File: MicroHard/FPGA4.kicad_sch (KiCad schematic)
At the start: 0 parts

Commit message: fpg
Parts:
- added U4: XC7A100T-FTG256, symbol FPGA_Xilinx_Artix7:XC7A100T-FTG256
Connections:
- new net +1V0: U4.F7 (VCCINT), U4.F9 (VCCINT), U4.G6 (VCCINT), U4.H9 (VCCINT), U4.J6 (VCCINT), U4.K9 (VCCINT), U4.L8 (VCCINT)
- new net GND: U4.A1 (GND), U4.A11 (GND), U4.B8 (GND), U4.C15 (GND), U4.C5 (GND), U4.D12 (GND), U4.D2 (GND), U4.E9 (GND), U4.F10 (GND), U4.F16 (GND), U4.F6 (GND), U4.G13 (GND), U4.G3 (GND), U4.G9 (GND), U4.H6 (GND), U4.J11 (GND), U4.J9 (GND), U4.K14 (GND), U4.K4 (GND), U4.K6 (GND), U4.L1 (GND), U4.L11 (GND), U4.M8 (GND), U4.N15 (GND), U4.N5 (GND), U4.P12 (GND), U4.P2 (GND), U4.R9 (GND), U4.T16 (GND), U4.T6 (GND)

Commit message: extra files
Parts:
- added C20: 330u, symbol Device:C_Polarized_US
- added C21, C22, C23, C24, C25, C26, C36, C37: 4.7u, symbol Device:C
- added C27, C28, C29, C30, C31, C32, C33, C34, C38, C39, C40, C42, C43: 470n, symbol Device:C
- added C35: 47u, symbol Device:C
- added C41: 100u, symbol Device:C_Polarized_US
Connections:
- net +1V0: now also U4.E10 (VCCBRAM), U4.F11 (VCCBRAM), C20.1, C21.1, C22.1, C23.1, C24.1, C25.1, C26.1, C27.1, C28.1, C29.1, C30.1, C31.1, C32.1, C33.1, C34.1, C41.1, C42.1, C43.1
- net GND: now also C20.2, C21.2, C22.2, C23.2, C24.2, C25.2, C26.2, C27.2, C28.2, C29.2, C30.2, C31.2, C32.2, C33.2, C34.2, C35.2, C36.2, C37.2, C38.2, C39.2, C40.2, C41.2, C42.2, C43.2
- net +1V8: now reaches U4.G10 (VCCAUX)
- net +1V8: now also U4.J10 (VCCAUX), U4.K11 (VCCAUX), U4.L10 (VCCAUX), C35.1, C36.1, C37.1, C38.1, C39.1, C40.1
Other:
- note added: "VCCAUX"
- note added: "VCCBRAM"
- note added: "VCCINT"
- moved on the sheet: U4D

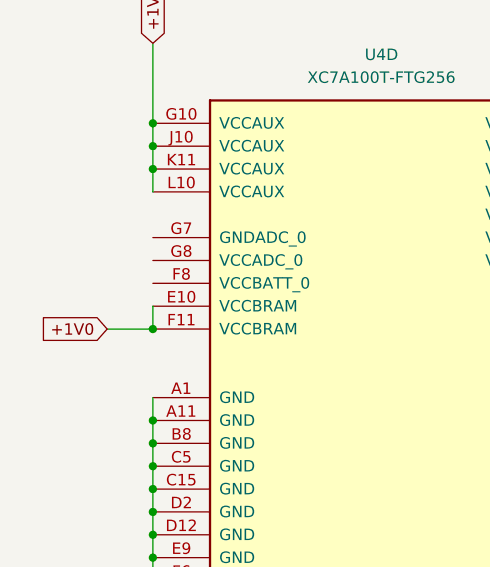
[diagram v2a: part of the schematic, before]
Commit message: feat: finished FPGA config
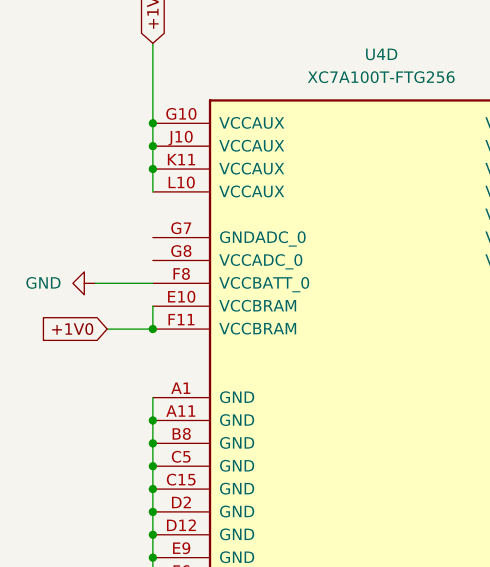
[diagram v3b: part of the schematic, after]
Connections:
- net GND: now also U4.F8 (VCCBATT_0)
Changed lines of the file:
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@@
+	(wire
+		(pts
+			(xy 24.13 76.2) (xy 30.48 76.2)
+		)
+		(stroke
+			(width 0)
+			(type default)
+		)
+	)
 	(wire
 		(pts
@@
 			)
 		)
+	)
+	(symbol
+		(lib_id "power:GND")
+		(at 24.13 76.2 270)
+		(unit 1)
+		(exclude_from_sim no)
+		(in_bom yes)
+		(on_board yes)
+		(dnp no)
+		(fields_autoplaced yes)
+		(property "Reference" "#PWR015"
+			(at 17.78 76.2 0)
+			(effects
+				(font
+					(size 1.27 1.27)
+				)
+				(hide yes)
+			)
+		)
+		(property "Value" "GND"
+			(at 20.32 76.1999 90)
+			(effects
+				(font
+					(size 1.27 1.27)
+				)
+				(justify right)
+			)
+		)
+		(property "Footprint" ""
+			(at 24.13 76.2 0)
+			(effects
+				(font
+					(size 1.27 1.27)
+				)
+				(hide yes)
+			)
+		)
+		(property "Datasheet" ""
+			(at 24.13 76.2 0)
+			(effects
+				(font
+					(size 1.27 1.27)
+				)
+				(hide yes)
+			)
+		)
+		(property "Description" "Power symbol creates a global label with name \"GND\" , ground"
+			(at 24.13 76.2 0)
+			(effects
+				(font
+					(size 1.27 1.27)
+				)
+				(hide yes)
+			)
+		)
+		(pin "1"
+		)
+		(instances
+			(project ""
+				(path "/578bd531-a491-4b15-a479-460d159ffc14/e381883e-e672-4900-88a5-08b94f970a88/ad62afa6-e46e-4108-a891-30710955bca2"
+					(reference "#PWR015")
+					(unit 1)
+				)
+			)
+		)

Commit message: feat: finished Flash mem and FPGA Config
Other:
- note added: "On the physical board the smallest capacitors must be closest to the power input"
- note removed: "VCCAUX"
- note removed: "VCCBRAM"
- note removed: "VCCINT"
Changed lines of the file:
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@@
+	(wire
+		(pts
+			(xy 99.06 85.09) (xy 109.22 85.09)
+		)
+		(stroke
+			(width 0)
+			(type default)
+		)
+	)
 	(wire
 		(pts
@@
 	(wire
 		(pts
+			(xy 97.79 119.38) (xy 109.22 119.38)
+		)
+		(stroke
+			(width 0)
+			(type default)
+		)
+	)
+	(wire
+		(pts
 			(xy 30.48 104.14) (xy 30.48 106.68)
 		)
@@
 	(wire
 		(pts
+			(xy 96.52 50.8) (xy 109.22 50.8)
+		)
+		(stroke
+			(width 0)
+			(type default)
+		)
+	)
+	(wire
+		(pts
 			(xy 81.28 104.14) (xy 81.28 106.68)
 		)
@@
 		)
 	)
-	(text "VCCINT\n"
+	(text "On the physical board the smallest capacitors must be closest to the power input\n"
 		(exclude_from_sim no)
-		(at 99.314 55.118 0)
-		(effects
-			(font
-				(size 1.27 1.27)
-			)
-		)
-	)
-	(text "VCCBRAM"
-		(exclude_from_sim no)
-		(at 98.806 124.206 0)
-		(effects
-			(font
-				(size 1.27 1.27)
-			)
-		)
-	)
-	(text "VCCAUX\n"
-		(exclude_from_sim no)
-		(at 99.314 89.154 0)
-		(effects
-			(font
-				(size 1.27 1.27)
-			)
-		)
-	)
-	(global_label "+1V0"
-		(shape input)
+		(at 171.958 46.228 0)
+		(effects
+			(font
+				(size 1.27 1.27)
+			)
+		)
+	)
+	(label "VCCINT"
+		(at 96.52 50.8 180)
+		(fields_autoplaced yes)
+		(effects
+			(font
+				(size 1.27 1.27)
+			)
+			(justify right bottom)
+		)
+	)
+	(label "VCCINT"
+		(at 81.28 49.53 90)
+		(fields_autoplaced yes)
+		(effects
+			(font
+				(size 1.27 1.27)
+			)
+			(justify left bottom)
+		)
+	)
+	(label "VCCAUX"
+		(at 99.06 85.09 180)
+		(fields_autoplaced yes)
+		(effects
+			(font
+				(size 1.27 1.27)
+			)
+			(justify right bottom)
+		)
+	)
+	(label "VCCBRAM"
 		(at 25.4 81.28 180)
 		(fields_autoplaced yes)
@@
 				(size 1.27 1.27)
 			)
-			(justify right)
-		)
-		(property "Intersheetrefs" "${INTERSHEET_REFS}"
-			(at 17.3348 81.28 0)
-			(effects
-				(font
-					(size 1.27 1.27)
-				)
-				(justify right)
-				(hide yes)
-			)
-		)
-	)
-	(global_label "+1V8"
-		(shape input)
+			(justify right bottom)
+		)
+	)
+	(label "VCCAUX"
 		(at 30.48 49.53 90)
 		(fields_autoplaced yes)
@@
 				(size 1.27 1.27)
 			)
-			(justify left)
-		)
-		(property "Intersheetrefs" "${INTERSHEET_REFS}"
-			(at 30.48 41.4648 90)
-			(effects
-				(font
-					(size 1.27 1.27)
-				)
-				(justify left)
-				(hide yes)
-			)
+			(justify left bottom)
+		)
+	)
+	(label "VCCBRAM"
+		(at 97.79 119.38 180)
+		(fields_autoplaced yes)
+		(effects
+			(font
+				(size 1.27 1.27)
+			)
+			(justify right bottom)
 		)
 	)
@@
 	(global_label "+1V0"
 		(shape input)
-		(at 81.28 49.53 90)
+		(at 109.22 48.26 90)
 		(fields_autoplaced yes)
 		(effects
@@
 		)
 		(property "Intersheetrefs" "${INTERSHEET_REFS}"
-			(at 81.28 41.4648 90)
+			(at 109.22 40.1948 90)
 			(effects
 				(font
@@
 			(effects
 				(font
-					(size 1.27 1.27)
-				)
-				(justify left)
-				(hide yes)
-			)
-		)
-	)
-	(global_label "+1V0"
-		(shape input)
-		(at 109.22 48.26 90)
-		(fields_autoplaced yes)
-		(effects
-			(font
-				(size 1.27 1.27)
-			)
-			(justify left)
-		)
-		(property "Intersheetrefs" "${INTERSHEET_REFS}"
-			(at 109.22 40.1948 90)
-			(effects
-				(font

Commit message: feat: VGA out lines from FPGA drawn
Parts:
- renumbered C20 to C57, C35 to C58, C41 to C59, C36 to C60, C21 to C61, C42 to C62, C37 to C63, C22 to C64, C43 to C65, C38 to C66, C23 to C67, C39 to C68, C24 to C69, C40 to C70, C25 to C71, C26 to C72, C27 to C73, C28 to C74, C29 to C75, C30 to C76, C31 to C77, C32 to C78, C33 to C79, C34 to C80, U4 to U5

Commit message: feat: finished schematic, TODO: go through checklist
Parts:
- U5: footprint (none) -> MicroHard:BGA256C100P16X16_1700X1700X155
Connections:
- net +1V8: now also U5.G8 (VCCADC_0)
- net GND: now also U5.G7 (GNDADC_0)
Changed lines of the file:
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@@
 	(wire
 		(pts
+			(xy 22.86 73.66) (xy 30.48 73.66)
+		)
+		(stroke
+			(width 0)
+			(type default)
+		)
+	)
+	(wire
+		(pts
 			(xy 109.22 115.57) (xy 109.22 119.38)
 		)
@@
 	(wire
 		(pts
+			(xy 24.13 71.12) (xy 30.48 71.12)
+		)
+		(stroke
+			(width 0)
+			(type default)
+		)
+	)
+	(wire
+		(pts
 			(xy 30.48 106.68) (xy 30.48 109.22)
 		)
@@
 		)
 	)
+	(global_label "+1V8"
+		(shape input)
+		(at 22.86 73.66 180)
+		(fields_autoplaced yes)
+		(effects
+			(font
+				(size 1.27 1.27)
+			)
+			(justify right)
+		)
+		(property "Intersheetrefs" "${INTERSHEET_REFS}"
+			(at 14.7948 73.66 0)
+			(effects
+				(font
+					(size 1.27 1.27)
+				)
+				(justify right)
+				(hide yes)
+			)
+		)
+	)
 	(symbol
 		(lib_id "power:GND")
@@
 			)
 		)
-		(property "Footprint" ""
+		(property "Footprint" "MicroHard:BGA256C100P16X16_1700X1700X155"
 			(at 55.88 91.44 0)
 			(effects
@@
 					(unit 1)
 				)
+			)
+		)
+	)
+	(symbol
+		(lib_id "power:GND")
+		(at 24.13 71.12 270)
+		(unit 1)
+		(exclude_from_sim no)
+		(in_bom yes)
+		(on_board yes)
+		(dnp no)
+		(fields_autoplaced yes)
+		(property "Reference" "#PWR062"
+			(at 17.78 71.12 0)
+			(effects
+				(font
+					(size 1.27 1.27)
+				)
+				(hide yes)
+			)
+		)
+		(property "Value" "GND"
+			(at 20.32 71.1199 90)
+			(effects
+				(font
+					(size 1.27 1.27)
+				)
+				(justify right)
+			)
+		)
+		(property "Footprint" ""
+			(at 24.13 71.12 0)
+			(effects
+				(font
+					(size 1.27 1.27)
+				)
+				(hide yes)
+			)
+		)
+		(property "Datasheet" ""
+			(at 24.13 71.12 0)
+			(effects
+				(font
+					(size 1.27 1.27)
+				)
+				(hide yes)
+			)
+		)
+		(property "Description" "Power symbol creates a global label with name \"GND\" , ground"
+			(at 24.13 71.12 0)
+			(effects
+				(font
+					(size 1.27 1.27)
+				)
+				(hide yes)
+			)
+		)
+		(pin "1"
+		)
+		(instances
+			(project "MicroHard"
+				(path "/578bd531-a491-4b15-a479-460d159ffc14/e381883e-e672-4900-88a5-08b94f970a88/ad62afa6-e46e-4108-a891-30710955bca2"
+					(reference "#PWR062")
+					(unit 1)
+				)

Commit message: Renumber parts
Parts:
- renumbered C57 to C48, C58 to C49, C59 to C50, C60 to C51, C61 to C52, C62 to C53, C63 to C54, C64 to C55, C65 to C56, C66 to C57, C67 to C58, C68 to C59, C69 to C60, C70 to C61, C71 to C62, C72 to C63, C73 to C64, C74 to C65, C75 to C66, C76 to C67, C77 to C68, C78 to C69, C79 to C70, C80 to C71, U5 to U4

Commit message: footprints
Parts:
- C48: footprint (none) -> Capacitor_Tantalum_SMD:CP_EIA-7343-31_Kemet-D_Pad2.25x2.55mm_HandSolder
- C49, C50: footprint (none) -> Capacitor_SMD:C_1210_3225Metric_Pad1.33x2.70mm_HandSolder
- C51, C52, C54, C55, C58, C60, C62, C63: footprint (none) -> Capacitor_SMD:C_0805_2012Metric_Pad1.18x1.45mm_HandSolder
- C53, C56, C57, C59, C61, C64, C65, C66, C67, C68, C69, C70, C71: footprint (none) -> Capacitor_SMD:C_0603_1608Metric_Pad1.08x0.95mm_HandSolder
